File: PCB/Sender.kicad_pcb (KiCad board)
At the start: 2 copper layers, 65 x 64.8 mm, 13 parts, among them J1 Screw_Terminal_01x08, J2 USB_B, U1 TLP291-4, U2 NodeMCU1.0(ESP-12E)

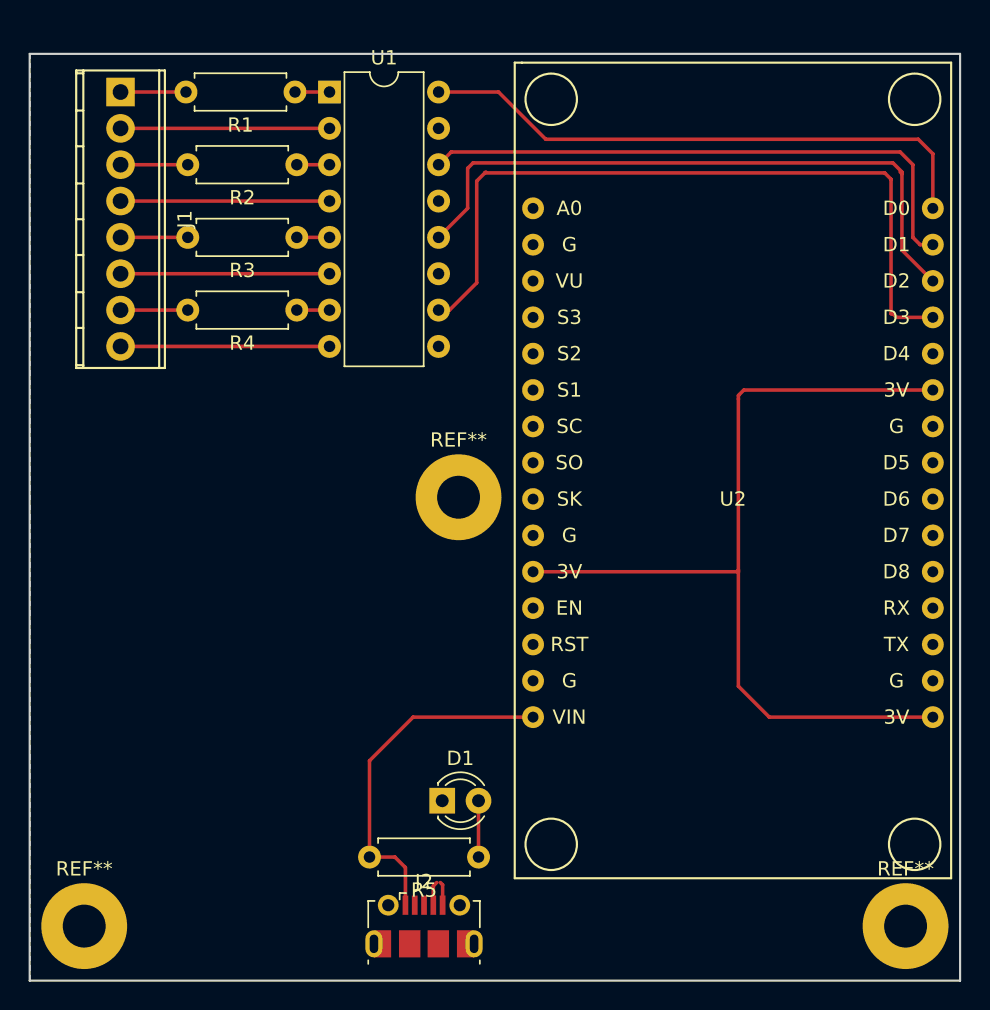
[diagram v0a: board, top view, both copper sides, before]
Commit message: Platine upgrade software change
Platine wurde angepasst mit einer schutzbeschaltung für die eingänge.

Sende program wurde eine auswertungder eingänge eingefügt

App wurde weiter entwickelt. es wird jetzt das wlan netz zum senden genutzt
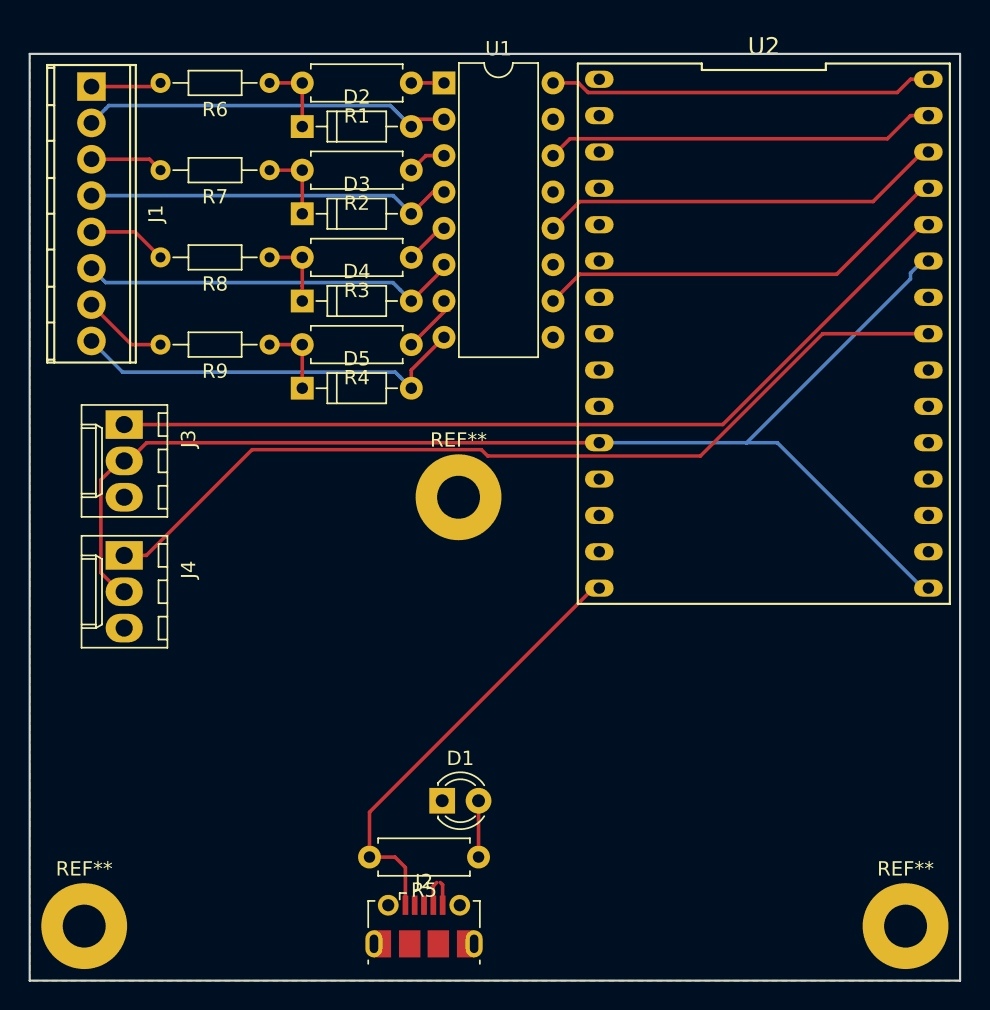
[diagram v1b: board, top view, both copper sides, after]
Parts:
- added D2: D_Zener, Diodes_THT:D_DO-35_SOD27_P7.62mm_Horizontal, F.Cu at (146.6, 58.2)
- added D3: D_Zener, Diodes_THT:D_DO-35_SOD27_P7.62mm_Horizontal, F.Cu at (146.6, 64.3)
- added D4: D_Zener, Diodes_THT:D_DO-35_SOD27_P7.62mm_Horizontal, F.Cu at (146.6, 70.4)
- added D5: D_Zener, Diodes_THT:D_DO-35_SOD27_P7.62mm_Horizontal, F.Cu at (146.6, 76.5)
- added J3: Conn_01x03_Male, Connectors_Molex:Molex_KK-6410-03_03x2.54mm_Straight, F.Cu at (134.1, 79.0)
- added J4: Conn_01x03_Male, Connectors_Molex:Molex_KK-6410-03_03x2.54mm_Straight, F.Cu at (134.1, 88.1)
- added R6: R, Resistors_THT:R_Axial_DIN0204_L3.6mm_D1.6mm_P7.62mm_Horizontal, F.Cu at (144.3, 55.1)
- added R7: R, Resistors_THT:R_Axial_DIN0204_L3.6mm_D1.6mm_P7.62mm_Horizontal, F.Cu at (144.3, 61.2)
- added R8: R, Resistors_THT:R_Axial_DIN0204_L3.6mm_D1.6mm_P7.62mm_Horizontal, F.Cu at (144.3, 67.3)
- added R9: R, Resistors_THT:R_Axial_DIN0204_L3.6mm_D1.6mm_P7.62mm_Horizontal, F.Cu at (144.3, 73.4)
- U2: footprint ESP8266:NodeMCU1.0(12-E) -> nodeMCU:DIP-30_1_ELL
- moved U2 11.8 mm to (178.8, 72.6), turned to 270 degrees
- moved R4 8.36 mm to (154.2, 73.4)
- moved R1 8.15 mm to (154.2, 55.1)
- moved R3 8.12 mm to (154.2, 67.3)
- moved U1 8.03 mm to (156.5, 55.1)
- moved R2 8.01 mm to (154.2, 61.2)
- moved J1 2.07 mm to (131.8, 55.4)
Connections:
- R1 pad 2: Net-(J1-Pad1) -> Net-(D2-Pad1)
- R2 pad 2: Net-(J1-Pad3) -> Net-(D3-Pad1)
- R3 pad 2: Net-(J1-Pad5) -> Net-(D4-Pad1)
- R4 pad 2: Net-(J1-Pad7) -> Net-(D5-Pad1)
- U2 pad 23: Net-(U2-Pad23) -> /D5
- U2 pad 26: Net-(U2-Pad26) -> /D4
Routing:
- net /D5: track 0.00 -> 63.3 mm
- net /D4: track 0.00 -> 62.0 mm
- net +3V3: track 63.0 -> 90.0 mm
- net /D3: track 52.5 -> 29.5 mm
- net /D2: track 45.1 -> 28.4 mm
- net Net-(D5-Pad2): track 14.6 -> 28.2 mm
- net /D0: track 40.1 -> 26.9 mm
- net /D1: track 40.6 -> 27.4 mm
- net Net-(D4-Pad2): track 14.6 -> 26.8 mm
- net Net-(D2-Pad2): track 14.6 -> 26.0 mm
- net Net-(D3-Pad2): track 14.6 -> 25.8 mm
- net +5V: track 24.9 -> 31.1 mm
- net Net-(D4-Pad1): track 0.00 -> 5.33 mm
- net Net-(D3-Pad1): track 0.00 -> 5.33 mm
- net Net-(D2-Pad1): track 0.00 -> 5.33 mm
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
